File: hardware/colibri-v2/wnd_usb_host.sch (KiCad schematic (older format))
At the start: 14 parts

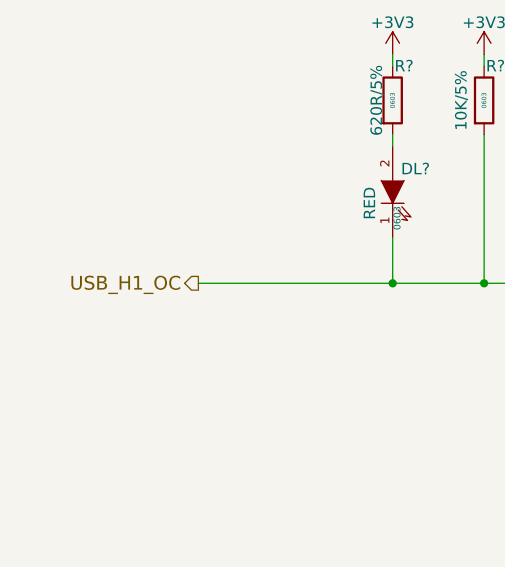
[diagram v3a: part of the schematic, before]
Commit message: Added ext_sensors.sch sheet
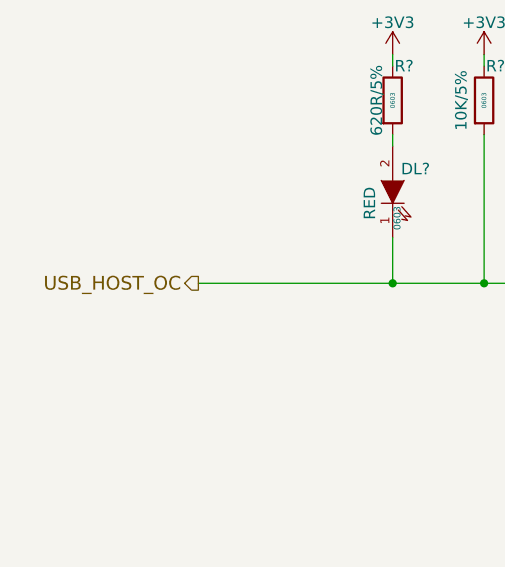
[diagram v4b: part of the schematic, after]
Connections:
- net USB_H1_OC renamed USB_HOST_OC
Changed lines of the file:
@@
 $Descr A4 11693 8268
 encoding utf-8
-Sheet 17 28
+Sheet 16 28
 Title ""
 Date ""
@@
 $EndComp
 Text HLabel 1900 2000 0    60   Output ~ 0
-USB_H1_OC
+USB_HOST_OC
 $Comp
 L +3V3 #PWR?

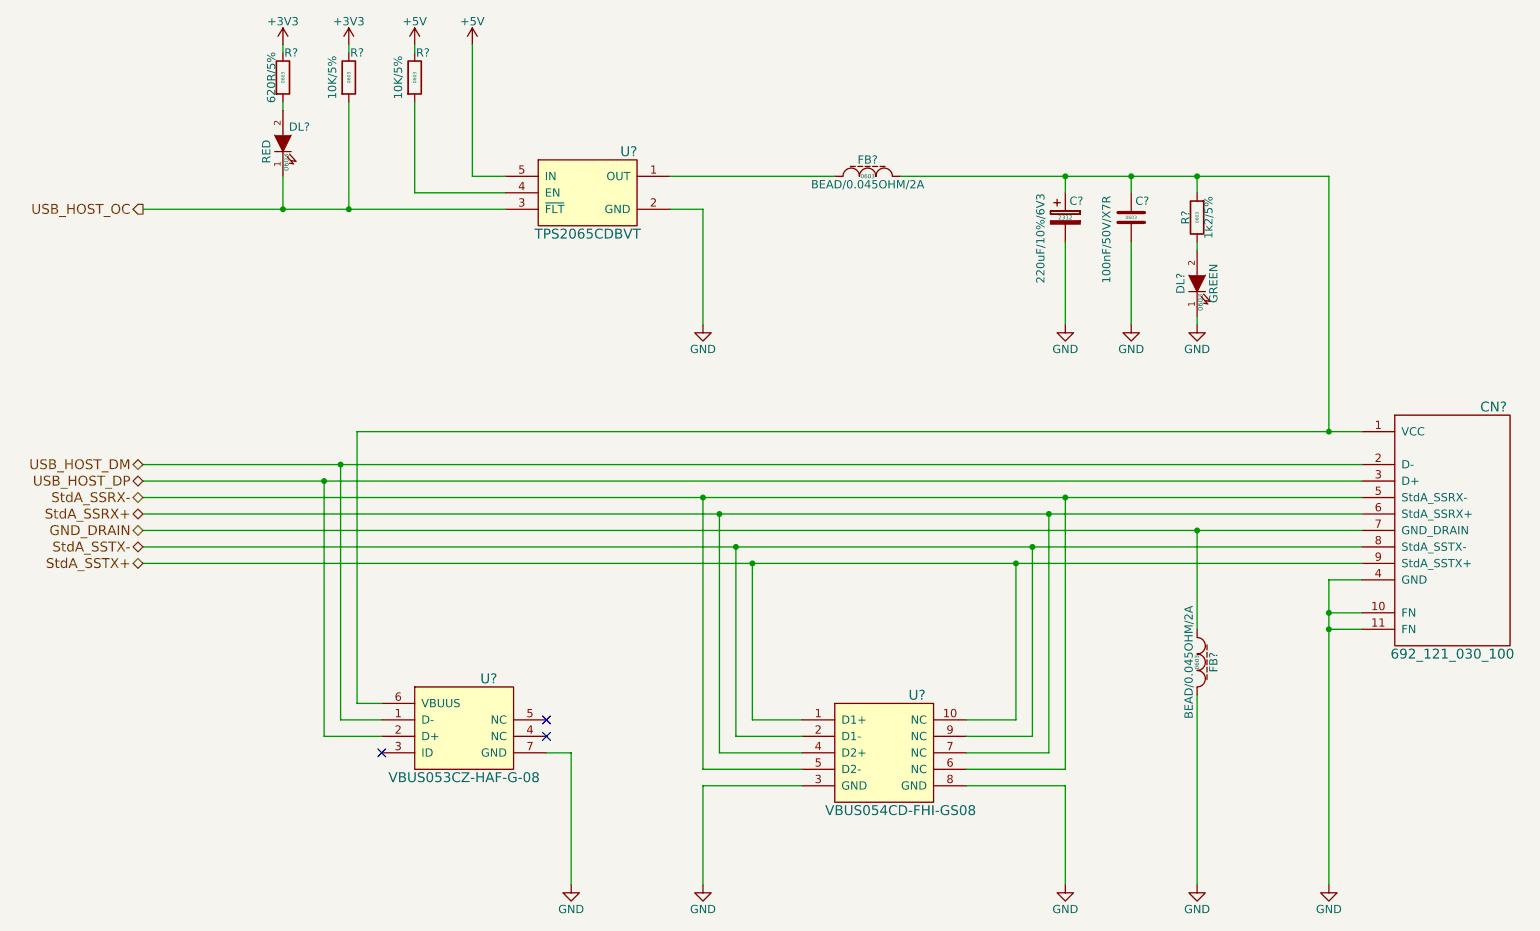
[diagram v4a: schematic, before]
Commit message: Resolving ERC problems
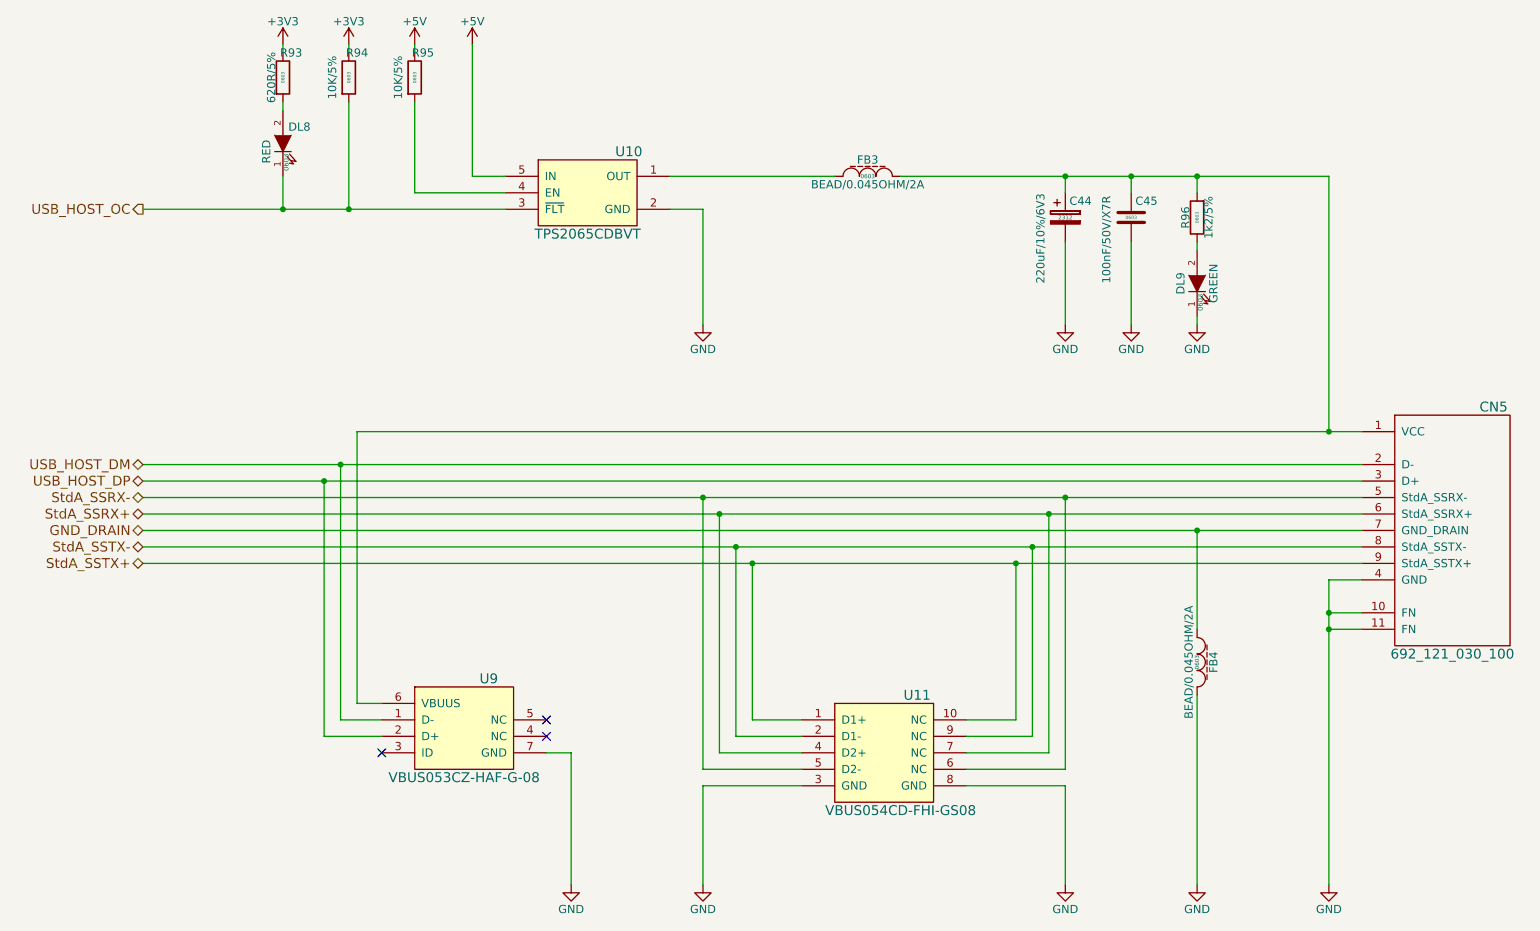
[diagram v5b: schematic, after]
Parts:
- gave numbers to parts that had none: 14
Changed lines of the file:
@@
 EESchema Schematic File Version 2
+LIBS:colibri-wnd-rescue
 LIBS:power
 LIBS:device
@@
 $EndDescr
 $Comp
-L VBUS053CZ-HAF-G-08 U?
+L VBUS053CZ-HAF-G-08 U9
 U 1 1 5619F269
 P 3850 5150
-F 0 "U?" H 4000 5450 60  0000 C CNN
+F 0 "U9" H 4000 5450 60  0000 C CNN
 F 1 "VBUS053CZ-HAF-G-08" H 3850 4850 60  0000 C CNN
 F 2 "" H 3800 5850 60  0001 C CNN
@@
 $EndComp
 $Comp
-L VBUS054CD-FHI-GS08 U?
+L VBUS054CD-FHI-GS08 U11
 U 1 1 5619FC64
 P 6400 5300
-F 0 "U?" H 6600 5650 60  0000 C CNN
+F 0 "U11" H 6600 5650 60  0000 C CNN
 F 1 "VBUS054CD-FHI-GS08" H 6500 4950 60  0000 C CNN
 F 2 "" H 6350 6000 60  0001 C CNN
@@
 $EndComp
 $Comp
-L 692_121_030_100 CN?
+L 692_121_030_100 CN5
 U 1 1 561A064E
 P 9850 3950
-F 0 "CN?" H 10100 4700 60  0000 C CNN
+F 0 "CN5" H 10100 4700 60  0000 C CNN
 F 1 "692_121_030_100" H 9850 3200 60  0000 C CNN
 F 2 "" H 9850 3950 60  0001 C CNN
@@
 USB_HOST_OC
 $Comp
-L +3V3 #PWR?
+L +3V3 #PWR0131
 U 1 1 561A1B20
 P 3150 1000
-F 0 "#PWR?" H 3150 850 50  0001 C CNN
+F 0 "#PWR0131" H 3150 850 50  0001 C CNN
 F 1 "+3V3" H 3150 1140 50  0000 C CNN
 F 2 "" H 3150 1000 60  0000 C CNN
@@
 $EndComp
 $Comp
-L +3V3 #PWR?
+L +3V3 #PWR0132
 U 1 1 561A1B3B
 P 2750 1000
-F 0 "#PWR?" H 2750 850 50  0001 C CNN
+F 0 "#PWR0132" H 2750 850 50  0001 C CNN
 F 1 "+3V3" H 2750 1140 50  0000 C CNN
 F 2 "" H 2750 1000 60  0000 C CNN
@@
 $EndComp
 $Comp
-L GND #PWR?
+L GND #PWR0133
 U 1 1 561A1B48
 P 7500 2700
-F 0 "#PWR?" H 7500 2450 50  0001 C CNN
+F 0 "#PWR0133" H 7500 2450 50  0001 C CNN
 F 1 "GND" H 7500 2550 50  0000 C CNN
 F 2 "" H 7500 2700 60  0000 C CNN
@@
 $EndComp
 $Comp
-L GND #PWR?
+L GND #PWR0134
 U 1 1 561A1B4E
 P 5300 2700
-F 0 "#PWR?" H 5300 2450 50  0001 C CNN
+F 0 "#PWR0134" H 5300 2450 50  0001 C CNN
 F 1 "GND" H 5300 2550 50  0000 C CNN
 F 2 "" H 5300 2700 60  0000 C CNN
@@
 $EndComp
 $Comp
-L +5V #PWR?
+L +5V #PWR0135
 U 1 1 561A1B64
 P 3900 1000
-F 0 "#PWR?" H 3900 850 50  0001 C CNN
+F 0 "#PWR0135" H 3900 850 50  0001 C CNN
 F 1 "+5V" H 3900 1140 50  0000 C CNN
 F 2 "" H 3900 1000 60  0000 C CNN
@@
 $EndComp
 $Comp
-L GND #PWR?
+L GND #PWR0136
 U 1 1 561A2244
 P 7900 2700
-F 0 "#PWR?" H 7900 2450 50  0001 C CNN
+F 0 "#PWR0136" H 7900 2450 50  0001 C CNN
 F 1 "GND" H 7900 2550 50  0000 C CNN
 F 2 "" H 7900 2700 60  0000 C CNN
@@
 StdA_SSTX+
 $Comp
-L GND #PWR?
+L GND #PWR0137
 U 1 1 561A3388
 P 8300 6100
-F 0 "#PWR?" H 8300 5850 50  0001 C CNN
+F 0 "#PWR0137" H 8300 5850 50  0001 C CNN
 F 1 "GND" H 8300 5950 50  0000 C CNN
 F 2 "" H 8300 6100 60  0000 C CNN
@@
 $EndComp
 $Comp
-L GND #PWR?
+L GND #PWR0138
 U 1 1 561A33B7
 P 7500 6100
-F 0 "#PWR?" H 7500 5850 50  0001 C CNN
+F 0 "#PWR0138" H 7500 5850 50  0001 C CNN
 F 1 "GND" H 7500 5950 50  0000 C CNN
 F 2 "" H 7500 6100 60  0000 C CNN
@@
 $EndComp
 $Comp
-L GND #PWR?
+L GND #PWR0139
 U 1 1 561A3438
 P 5300 6100
-F 0 "#PWR?" H 5300 5850 50  0001 C CNN
+F 0 "#PWR0139" H 5300 5850 50  0001 C CNN
 F 1 "GND" H 5300 5950 50  0000 C CNN
 F 2 "" H 5300 6100 60  0000 C CNN
@@
 	3200 5000 3200 3350
 $Comp
-L GND #PWR?
+L GND #PWR0140
 U 1 1 561A6CE3
 P 4500 6100
-F 0 "#PWR?" H 4500 5850 50  0001 C CNN
+F 0 "#PWR0140" H 4500 5850 50  0001 C CNN
 F 1 "GND" H 4500 5950 50  0000 C CNN
 F 2 "" H 4500 6100 60  0000 C CNN
@@
 NoConn ~ 3350 5300
 $Comp
-L GND #PWR?
+L GND #PWR0141
 U 1 1 561A74D9
 P 9100 6100
-F 0 "#PWR?" H 9100 5850 50  0001 C CNN
+F 0 "#PWR0141" H 9100 5850 50  0001 C CNN
 F 1 "GND" H 9100 5950 50  0000 C CNN
 F 2 "" H 9100 6100 60  0000 C CNN
@@
 Connection ~ 9100 4550
 $Comp
-L R_SMT R?
+L R_SMT R93
 U 1 1 563513C2
 P 2750 1200
-F 0 "R?" H 2800 1350 50  0000 C CNN
+F 0 "R93" H 2800 1350 50  0000 C CNN
 F 1 "620R/5%" V 2680 1200 50  0000 C CNN
 F 2 "Resistors_SMD:R_0603" V 2900 1200 30  0001 C CNN
@@
 $EndComp
 $Comp
-L LED_SMT DL?
+L LED_SMT DL8
 U 1 1 563518B5
 P 2750 1600
-F 0 "DL?" V 2850 1500 50  0000 C CNN
+F 0 "DL8" V 2850 1500 50  0000 C CNN
 F 1 "RED" H 2700 1700 50  0000 C CNN
 F 2 "LEDs:LED-0603" H 2750 1450 30  0001 C CNN
@@
 $EndComp
 $Comp
-L R_SMT R?
+L R_SMT R95
 U 1 1 563526BF
 P 3550 1200
-F 0 "R?" H 3600 1350 50  0000 C CNN
+F 0 "R95" H 3600 1350 50  0000 C CNN
 F 1 "10K/5%" V 3450 1200 50  0000 C CNN
 F 2 "Resistors_SMD:R_0603" V 3700 1200 30  0001 C CNN
@@
 $EndComp
 $Comp
-L CP_SMT C?
+L CP_SMT C44
 U 1 1 5635343E
 P 7500 2050
-F 0 "C?" H 7525 2150 50  0000 L CNN
+F 0 "C44" H 7525 2150 50  0000 L CNN
 F 1 "220uF/10%/6V3" V 7350 1650 50  0000 L CNN
 F 2 "Capacitors_Tantalum_SMD:TantalC_SizeC_EIA-6032_Reflow" H 7538 1900 30  0001 C CNN
@@
 $EndComp
 $Comp
-L C_SMT C?
+L C_SMT C45
 U 1 1 563526B5
 P 7900 2050
-F 0 "C?" H 7925 2150 50  0000 L CNN
+F 0 "C45" H 7925 2150 50  0000 L CNN
 F 1 "100nF/50V/X7R" V 7750 1650 50  0000 L CNN
 F 2 "Capacitors_SMD:C_0603" H 7930 1900 30  0001 L CNN
@@
 $EndComp
 $Comp
-L FB_SMT FB?
+L FB_SMT FB3
 U 1 1 56353A77
 P 6300 1800
-F 0 "FB?" H 6300 1900 50  0000 C CNN
+F 0 "FB3" H 6300 1900 50  0000 C CNN
 F 1 "BEAD/0.045OHM/2A" H 6300 1750 50  0000 C CNN
 F 2 "Resistors_SMD:R_0603" H 6300 1700 30  0001 C CNN
@@
 $EndComp
 $Comp
-L FB_SMT FB?
+L FB_SMT FB4
 U 1 1 56354381
 P 8300 4750
-F 0 "FB?" H 8300 4850 50  0000 C CNN
+F 0 "FB4" H 8300 4850 50  0000 C CNN
 F 1 "BEAD/0.045OHM/2A" H 8300 4700 50  0000 C CNN
 F 2 "Resistors_SMD:R_0603" H 8300 4650 30  0001 C CNN
@@
 $EndComp
 $Comp
-L TPS2065CDBVT U?
+L TPS2065CDBVT U10
 U 1 1 563650DC
 P 4600 1900
-F 0 "U?" H 4850 2150 60  0000 C CNN
+F 0 "U10" H 4850 2150 60  0000 C CNN
 F 1 "TPS2065CDBVT" H 4600 1650 60  0000 C CNN
 F 2 "" H 4600 1700 60  0000 C CNN
@@
 $EndComp
 $Comp
-L +5V #PWR?
+L +5V #PWR0142
 U 1 1 56365222
 P 3550 1000
-F 0 "#PWR?" H 3550 850 50  0001 C CNN
+F 0 "#PWR0142" H 3550 850 50  0001 C CNN
 F 1 "+5V" H 3550 1140 50  0000 C CNN
 F 2 "" H 3550 1000 60  0000 C CNN
@@
 	3550 1900 4100 1900
 $Comp
-L R_SMT R?
+L R_SMT R94
 U 1 1 563654E4
 P 3150 1200
-F 0 "R?" H 3200 1350 50  0000 C CNN
+F 0 "R94" H 3200 1350 50  0000 C CNN
 F 1 "10K/5%" V 3050 1200 50  0000 C CNN
 F 2 "Resistors_SMD:R_0603" V 3300 1200 30  0001 C CNN
@@
 $EndComp
 $Comp
-L R_SMT R?
+L R_SMT R96
 U 1 1 56366BD8
 P 8300 2050
-F 0 "R?" V 8370 2050 50  0000 C CNN
+F 0 "R96" V 8370 2050 50  0000 C CNN
 F 1 "1k2/5%" V 8230 2050 50  0000 C CNN
 F 2 "Resistors_SMD:R_0603" V 8450 2050 30  0001 C CNN
@@
 $EndComp
 $Comp
-L LED_SMT DL?
+L LED_SMT DL9
 U 1 1 56366BE2
 P 8300 2450
-F 0 "DL?" H 8300 2550 50  0000 C CNN
+F 0 "DL9" H 8300 2550 50  0000 C CNN
 F 1 "GREEN" H 8300 2350 50  0000 C CNN
 F 2 "LEDs:LED-0603" H 8300 2300 30  0001 C CNN
@@
 $EndComp
 $Comp
-L GND #PWR?
+L GND #PWR0143
 U 1 1 56366BE9
 P 8300 2700
-F 0 "#PWR?" H 8300 2450 50  0001 C CNN
+F 0 "#PWR0143" H 8300 2450 50  0001 C CNN
 F 1 "GND" H 8300 2550 50  0000 C CNN
 F 2 "" H 8300 2700 60  0000 C CNN

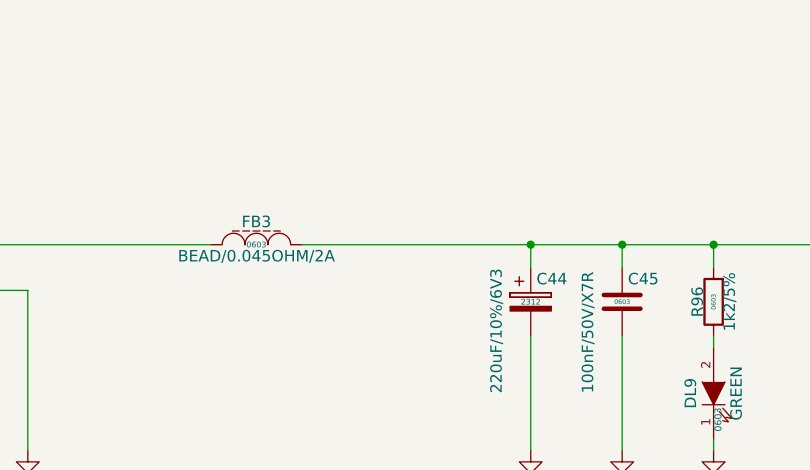
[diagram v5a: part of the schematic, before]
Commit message: Fixed ERC errors
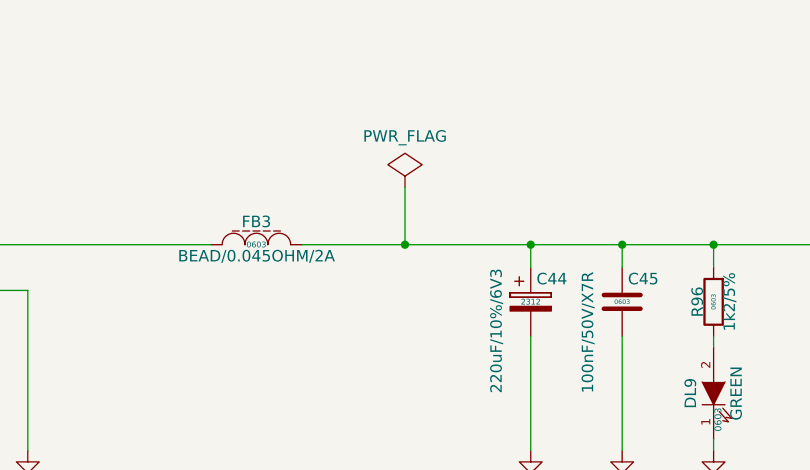
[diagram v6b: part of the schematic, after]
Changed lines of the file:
@@
 USB_HOST_OC
 $Comp
-L +3V3 #PWR0131
+L +3V3 #PWR0133
 U 1 1 561A1B20
 P 3150 1000
-F 0 "#PWR0131" H 3150 850 50  0001 C CNN
+F 0 "#PWR0133" H 3150 850 50  0001 C CNN
 F 1 "+3V3" H 3150 1140 50  0000 C CNN
 F 2 "" H 3150 1000 60  0000 C CNN
@@
 $EndComp
 $Comp
-L +3V3 #PWR0132
+L +3V3 #PWR0134
 U 1 1 561A1B3B
 P 2750 1000
-F 0 "#PWR0132" H 2750 850 50  0001 C CNN
+F 0 "#PWR0134" H 2750 850 50  0001 C CNN
 F 1 "+3V3" H 2750 1140 50  0000 C CNN
 F 2 "" H 2750 1000 60  0000 C CNN
@@
 $EndComp
 $Comp
-L GND #PWR0133
+L GND #PWR0135
 U 1 1 561A1B48
 P 7500 2700
-F 0 "#PWR0133" H 7500 2450 50  0001 C CNN
+F 0 "#PWR0135" H 7500 2450 50  0001 C CNN
 F 1 "GND" H 7500 2550 50  0000 C CNN
 F 2 "" H 7500 2700 60  0000 C CNN
@@
 $EndComp
 $Comp
-L GND #PWR0134
+L GND #PWR0136
 U 1 1 561A1B4E
 P 5300 2700
-F 0 "#PWR0134" H 5300 2450 50  0001 C CNN
+F 0 "#PWR0136" H 5300 2450 50  0001 C CNN
 F 1 "GND" H 5300 2550 50  0000 C CNN
 F 2 "" H 5300 2700 60  0000 C CNN
@@
 $EndComp
 $Comp
-L +5V #PWR0135
+L +5V #PWR0137
 U 1 1 561A1B64
 P 3900 1000
-F 0 "#PWR0135" H 3900 850 50  0001 C CNN
+F 0 "#PWR0137" H 3900 850 50  0001 C CNN
 F 1 "+5V" H 3900 1140 50  0000 C CNN
 F 2 "" H 3900 1000 60  0000 C CNN
@@
 $EndComp
 $Comp
-L GND #PWR0136
+L GND #PWR0138
 U 1 1 561A2244
 P 7900 2700
-F 0 "#PWR0136" H 7900 2450 50  0001 C CNN
+F 0 "#PWR0138" H 7900 2450 50  0001 C CNN
 F 1 "GND" H 7900 2550 50  0000 C CNN
 F 2 "" H 7900 2700 60  0000 C CNN
@@
 StdA_SSTX+
 $Comp
-L GND #PWR0137
+L GND #PWR0139
 U 1 1 561A3388
 P 8300 6100
-F 0 "#PWR0137" H 8300 5850 50  0001 C CNN
+F 0 "#PWR0139" H 8300 5850 50  0001 C CNN
 F 1 "GND" H 8300 5950 50  0000 C CNN
 F 2 "" H 8300 6100 60  0000 C CNN
@@
 $EndComp
 $Comp
-L GND #PWR0138
+L GND #PWR0140
 U 1 1 561A33B7
 P 7500 6100
-F 0 "#PWR0138" H 7500 5850 50  0001 C CNN
+F 0 "#PWR0140" H 7500 5850 50  0001 C CNN
 F 1 "GND" H 7500 5950 50  0000 C CNN
 F 2 "" H 7500 6100 60  0000 C CNN
@@
 $EndComp
 $Comp
-L GND #PWR0139
+L GND #PWR0141
 U 1 1 561A3438
 P 5300 6100
-F 0 "#PWR0139" H 5300 5850 50  0001 C CNN
+F 0 "#PWR0141" H 5300 5850 50  0001 C CNN
 F 1 "GND" H 5300 5950 50  0000 C CNN
 F 2 "" H 5300 6100 60  0000 C CNN
@@
 	3200 5000 3200 3350
 $Comp
-L GND #PWR0140
+L GND #PWR0142
 U 1 1 561A6CE3
 P 4500 6100
-F 0 "#PWR0140" H 4500 5850 50  0001 C CNN
+F 0 "#PWR0142" H 4500 5850 50  0001 C CNN
 F 1 "GND" H 4500 5950 50  0000 C CNN
 F 2 "" H 4500 6100 60  0000 C CNN
@@
 NoConn ~ 3350 5300
 $Comp
-L GND #PWR0141
+L GND #PWR0143
 U 1 1 561A74D9
 P 9100 6100
-F 0 "#PWR0141" H 9100 5850 50  0001 C CNN
+F 0 "#PWR0143" H 9100 5850 50  0001 C CNN
 F 1 "GND" H 9100 5950 50  0000 C CNN
 F 2 "" H 9100 6100 60  0000 C CNN
@@
 $EndComp
 $Comp
-L +5V #PWR0142
+L +5V #PWR0144
 U 1 1 56365222
 P 3550 1000
-F 0 "#PWR0142" H 3550 850 50  0001 C CNN
+F 0 "#PWR0144" H 3550 850 50  0001 C CNN
 F 1 "+5V" H 3550 1140 50  0000 C CNN
 F 2 "" H 3550 1000 60  0000 C CNN
@@
 $EndComp
 $Comp
-L GND #PWR0143
+L GND #PWR0145
 U 1 1 56366BE9
 P 8300 2700
-F 0 "#PWR0143" H 8300 2450 50  0001 C CNN
+F 0 "#PWR0145" H 8300 2450 50  0001 C CNN
 F 1 "GND" H 8300 2550 50  0000 C CNN
 F 2 "" H 8300 2700 60  0000 C CNN
@@
 	8300 1800 8300 1900
 Connection ~ 8300 1800
+$Comp
+L PWR_FLAG #FLG0146
+U 1 1 56CB7F4B
+P 6950 1550
+F 0 "#FLG0146" H 6950 1645 50  0001 C CNN
+F 1 "PWR_FLAG" H 6950 1774 50  0000 C CNN
+F 2 "" H 6950 1550 50  0000 C CNN
+F 3 "" H 6950 1550 50  0000 C CNN
+	1    6950 1550
+	1    0    0    -1
+$EndComp
+Wire Wire Line
+	6950 1550 6950 1800
+Connection ~ 6950 1800
 $EndSCHEMATC
